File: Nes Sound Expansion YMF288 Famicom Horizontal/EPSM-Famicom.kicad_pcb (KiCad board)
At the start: 4 copper layers, 99 x 91.7 mm, 60 parts, among them J1 CARTRIDGE_F, J2 OUT_1, J3 EPSM_ADDRESSING, J4 CONSOLE_M, J5 AudioJack4_SwitchTR1, U1 74LS174, U10 74LS257, U2 74LS174, U3 74LS139, U4 74LS132, U5 YMF288, U6 BU9480F, U7 74LS257, U8 74LS257, U9 LM358, X1 SG-8002CA

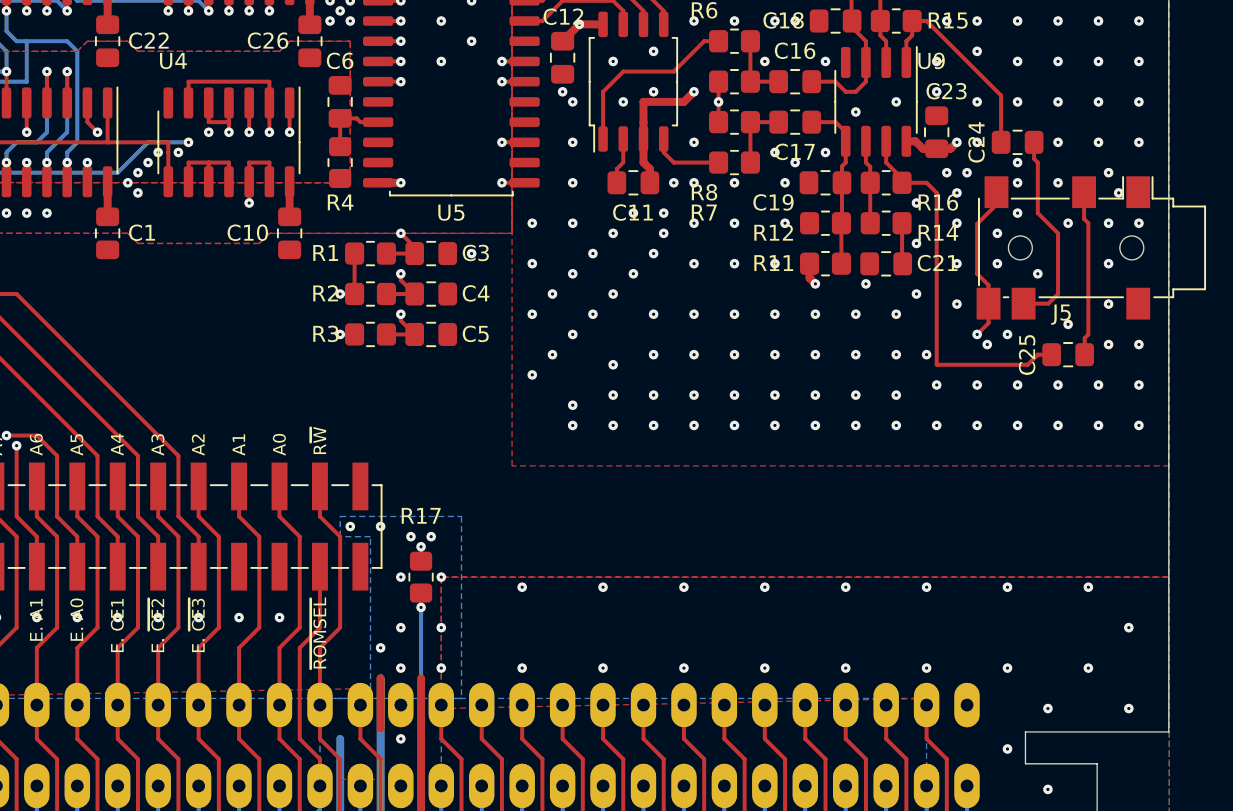
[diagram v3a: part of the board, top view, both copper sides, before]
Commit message: Clarify EPSM chip enable and address net names
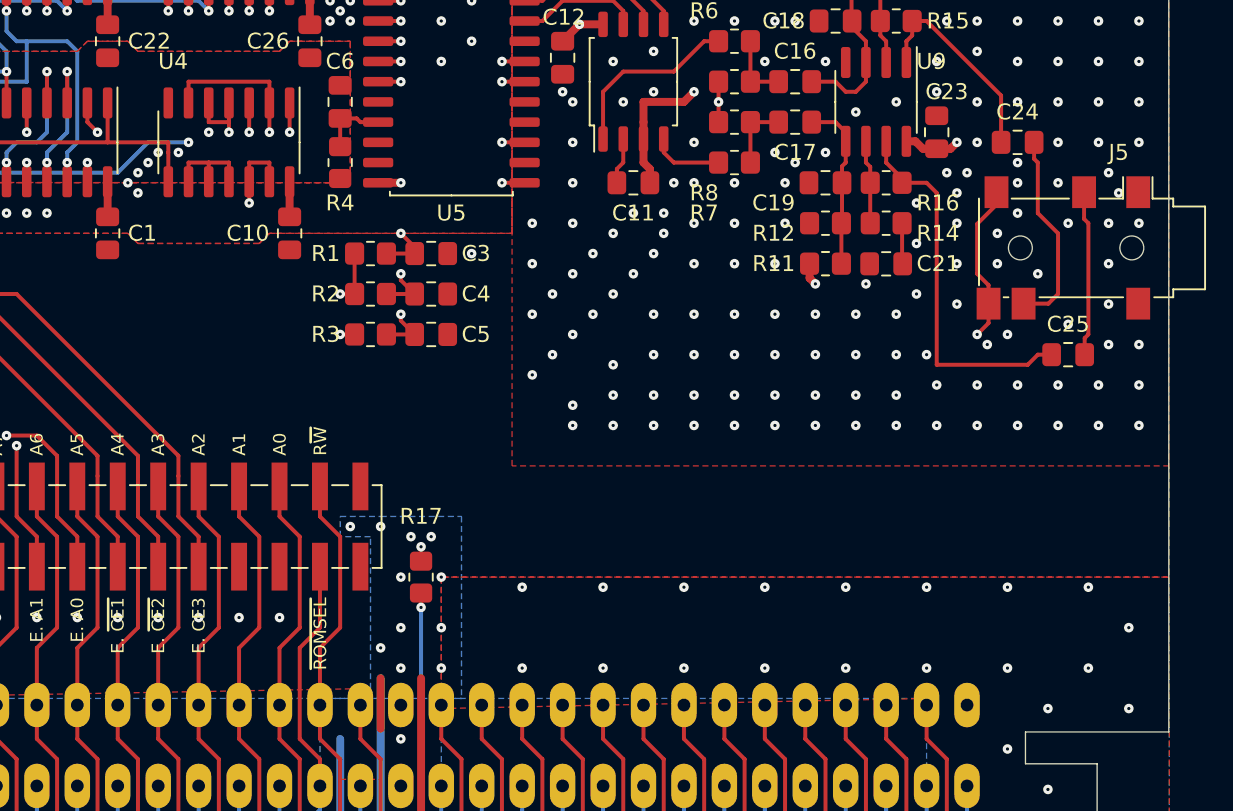
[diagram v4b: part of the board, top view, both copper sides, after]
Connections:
- net /EPSM_A0_A13 renamed /EPSM_A0
- net /EPSM_A1_A1 renamed /EPSM_A1
- net /EPSM_CE1_A14 renamed /EPSM_~{CE1}
- net /EPSM_CE2_~{ROMSEL} renamed /EPSM_~{CE2}
- net /EPSM_CE3_CPU_R~{W} renamed /EPSM_CE3
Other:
- board text added: "VCC M2 A12 A13 A14 E. A1 E. A0 E. ~{CE1} E. ~{CE2} E. CE3 ~{ROMSEL}"
- board text removed: "VCC M2 A12 A13 A14 E. A1 E. A0 E. CE1 E. ~{CE2} E. ~{CE3} ~{ROMSEL}"
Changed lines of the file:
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@@
   (net 62 "/OUT_1")
   (net 63 "unconnected-(J3-Pad24)")
-  (net 64 "/EPSM_A1_A1")
-  (net 65 "/EPSM_A0_A13")
-  (net 66 "/EPSM_CE1_A14")
-  (net 67 "/EPSM_CE2_~{ROMSEL}")
-  (net 68 "/EPSM_CE3_CPU_R~{W}")
+  (net 64 "/EPSM_A1")
+  (net 65 "/EPSM_A0")
+  (net 66 "/EPSM_~{CE1}")
+  (net 67 "/EPSM_~{CE2}")
+  (net 68 "/EPSM_CE3")
   (net 69 "unconnected-(J3-Pad26)")
   (net 70 "unconnected-(J3-Pad29)")
@@
     (fp_line (start -0.975 -4.95) (end 1.95 -4.95) (layer "F.Fab") (width 0.1))
     (pad "1" smd roundrect (at -2.475 -4.445 270) (size 1.95 0.6) (layers "F.Cu" "F.Paste" "F.Mask") (roundrect_rratio 0.25)
-      (net 67 "/EPSM_CE2_~{ROMSEL}") (pinfunction "E") (pintype "input"))
+      (net 67 "/EPSM_~{CE2}") (pinfunction "E") (pintype "input"))
     (pad "2" smd roundrect (at -2.475 -3.175 270) (size 1.95 0.6) (layers "F.Cu" "F.Paste" "F.Mask") (roundrect_rratio 0.25)
-      (net 66 "/EPSM_CE1_A14") (pinfunction "A0") (pintype "input"))
+      (net 66 "/EPSM_~{CE1}") (pinfunction "A0") (pintype "input"))
     (pad "3" smd roundrect (at -2.475 -1.905 270) (size 1.95 0.6) (layers "F.Cu" "F.Paste" "F.Mask") (roundrect_rratio 0.25)
-      (net 68 "/EPSM_CE3_CPU_R~{W}") (pinfunction "A1") (pintype "input"))
+      (net 68 "/EPSM_CE3") (pinfunction "A1") (pintype "input"))
     (pad "4" smd roundrect (at -2.475 -0.635 270) (size 1.95 0.6) (layers "F.Cu" "F.Paste" "F.Mask") (roundrect_rratio 0.25)
       (net 76 "unconnected-(U3-Pad4)") (pinfunction "O0") (pintype "output+no_connect"))
@@
       (net 7 "/CPU_A6") (pinfunction "Pin_13") (pintype "passive"))
     (pad "14" smd rect (at -2.52 -2.54 90) (size 3 1) (layers "F.Cu" "F.Paste" "F.Mask")
-      (net 64 "/EPSM_A1_A1") (pinfunction "Pin_14") (pintype "passive"))
+      (net 64 "/EPSM_A1") (pinfunction "Pin_14") (pintype "passive"))
     (pad "15" smd rect (at 2.52 0 90) (size 3 1) (layers "F.Cu" "F.Paste" "F.Mask")
       (net 8 "/CPU_A5") (pinfunction "Pin_15") (pintype "passive"))
     (pad "16" smd rect (at -2.52 0 90) (size 3 1) (layers "F.Cu" "F.Paste" "F.Mask")
-      (net 65 "/EPSM_A0_A13") (pinfunction "Pin_16") (pintype "passive"))
+      (net 65 "/EPSM_A0") (pinfunction "Pin_16") (pintype "passive"))
     (pad "17" smd rect (at 2.52 2.54 90) (size 3 1) (layers "F.Cu" "F.Paste" "F.Mask")
       (net 9 "/CPU_A4") (pinfunction "Pin_17") (pintype "passive"))
     (pad "18" smd rect (at -2.52 2.54 90) (size 3 1) (layers "F.Cu" "F.Paste" "F.Mask")
-      (net 66 "/EPSM_CE1_A14") (pinfunction "Pin_18") (pintype "passive"))
+      (net 66 "/EPSM_~{CE1}") (pinfunction "Pin_18") (pintype "passive"))
     (pad "19" smd rect (at 2.52 5.08 90) (size 3 1) (layers "F.Cu" "F.Paste" "F.Mask")
       (net 10 "/CPU_A3") (pinfunction "Pin_19") (pintype "passive"))
     (pad "20" smd rect (at -2.52 5.08 90) (size 3 1) (layers "F.Cu" "F.Paste" "F.Mask")
-      (net 67 "/EPSM_CE2_~{ROMSEL}") (pinfunction "Pin_20") (pintype "passive"))
+      (net 67 "/EPSM_~{CE2}") (pinfunction "Pin_20") (pintype "passive"))
     (pad "21" smd rect (at 2.52 7.62 90) (size 3 1) (layers "F.Cu" "F.Paste" "F.Mask")
       (net 11 "/CPU_A2") (pinfunction "Pin_21") (pintype "passive"))
     (pad "22" smd rect (at -2.52 7.62 90) (size 3 1) (layers "F.Cu" "F.Paste" "F.Mask")
-      (net 68 "/EPSM_CE3_CPU_R~{W}") (pinfunction "Pin_22") (pintype "passive"))
+      (net 68 "/EPSM_CE3") (pinfunction "Pin_22") (pintype "passive"))
     (pad "23" smd rect (at 2.52 10.16 90) (size 3 1) (layers "F.Cu" "F.Paste" "F.Mask")
       (net 12 "/CPU_A1") (pinfunction "Pin_23") (pintype "passive"))
@@
     (property "Sheetname" "")
     (attr smd)
-    (fp_text reference "C25" (at -2.54 0 90) (layer "F.SilkS")
+    (fp_text reference "C25" (at 0 -1.905 180) (layer "F.SilkS")
       (effects (font (size 1 1) (thickness 0.15)))
     )
@@
     (property "Sheetname" "")
     (attr smd)
-    (fp_text reference "J5" (at 4.09 6.955) (layer "F.SilkS")
+    (fp_text reference "J5" (at -5.995 3.425) (layer "F.SilkS")
       (effects (font (size 1 1) (thickness 0.15)))
     )
@@
       (net 73 "/$4016_EN") (pinfunction "S") (pintype "input"))
     (pad "2" smd roundrect (at -2.475 -3.175 270) (size 1.95 0.6) (layers "F.Cu" "F.Paste" "F.Mask") (roundrect_rratio 0.25)
-      (net 64 "/EPSM_A1_A1") (pinfunction "I0a") (pintype "input"))
+      (net 64 "/EPSM_A1") (pinfunction "I0a") (pintype "input"))
     (pad "3" smd roundrect (at -2.475 -1.905 270) (size 1.95 0.6) (layers "F.Cu" "F.Paste" "F.Mask") (roundrect_rratio 0.25)
       (net 107 "/BUF_A0") (pinfunction "I1a") (pintype "input"))
@@
       (net 108 "/YM_A1") (pinfunction "Za") (pintype "tri_state"))
     (pad "5" smd roundrect (at -2.475 0.635 270) (size 1.95 0.6) (layers "F.Cu" "F.Paste" "F.Mask") (roundrect_rratio 0.25)
-      (net 65 "/EPSM_A0_A13") (pinfunction "I0b") (pintype "input"))
+      (net 65 "/EPSM_A0") (pinfunction "I0b") (pintype "input"))
     (pad "6" smd roundrect (at -2.475 1.905 270) (size 1.95 0.6) (layers "F.Cu" "F.Paste" "F.Mask") (roundrect_rratio 0.25)
       (net 105 "/BUF_A1") (pinfunction "I1b") (pintype "input"))
@@
     (property "Sheetname" "")
     (attr smd)
-    (fp_text reference "C24" (at -2.54 0 90) (layer "F.SilkS")
+    (fp_text reference "C24" (at 0 -1.905 180) (layer "F.SilkS")
       (effects (font (size 1 1) (thickness 0.15)))
     )
@@
     (effects (font (size 1 1) (thickness 0.15)) (justify mirror))
   )
-  (gr_text "VCC\n\nM2\n\nA12\n\nA13\n\nA14\n\n \n\nE. A1\n\nE. A0\n\nE. CE1\n\nE. ~{CE2}\n\nE. ~{CE3}\n\n \n\n \n\n~{ROMSEL}\n\n " (at 107.95 93.345 90) (layer "F.SilkS")
+  (gr_text "VCC\n\nM2\n\nA12\n\nA13\n\nA14\n\n \n\nE. A1\n\nE. A0\n\nE. ~{CE1}\n\nE. ~{CE2}\n\nE. CE3\n\n \n\n \n\n~{ROMSEL}\n\n " (at 107.95 93.345 90) (layer "F.SilkS")
     (effects (font (size 0.79 0.8) (thickness 0.15875)) (justify right))
   )
@@
   (segment (start 110.49 89.535) (end 109.22 88.265) (width 0.25) (layer "F.Cu") (net 66))
   (segment (start 95.885 77.47) (end 95.25 76.835) (width 0.25) (layer "F.Cu") (net 66))
-  (segment (start 109.22 88.265) (end 109.22 84.455) (width 0.25) (layer "F.Cu") (net 66))
+  (segment (start 109.22 85.725) (end 109.22 84.455) (width 0.25) (layer "F.Cu") (net 66))
+  (segment (start 109.22 88.265) (end 109.22 85.725) (width 0.25) (layer "F.Cu") (net 66))
   (segment (start 96.52 75.63) (end 102.935 75.63) (width 0.25) (layer "F.Cu") (net 67))
-  (segment (start 111.76 84.455) (end 111.76 88.265) (width 0.25) (layer "F.Cu") (net 67))
   (segment (start 102.935 75.63) (end 111.76 84.455) (width 0.25) (layer "F.Cu") (net 67))
   (segment (start 111.76 88.265) (end 113.03 89.535) (width 0.25) (layer "F.Cu") (net 67))
   (segment (start 113.03 89.535) (end 113.03 91.42) (width 0.25) (layer "F.Cu") (net 67))
+  (segment (start 111.76 84.455) (end 111.76 85.725) (width 0.25) (layer "F.Cu") (net 67))
+  (segment (start 111.76 85.725) (end 111.76 88.265) (width 0.25) (layer "F.Cu") (net 67))
   (segment (start 96.52 74.295) (end 104.14 74.295) (width 0.25) (layer "F.Cu") (net 68))
-  (segment (start 114.3 84.455) (end 114.3 88.265) (width 0.25) (layer "F.Cu") (net 68))
+  (segment (start 114.3 84.455) (end 114.3 85.725) (width 0.25) (layer "F.Cu") (net 68))
+  (segment (start 114.3 85.725) (end 114.3 88.265) (width 0.25) (layer "F.Cu") (net 68))
   (segment (start 93.98 75.63) (end 93.98 74.295) (width 0.25) (layer "F.Cu") (net 68))
   (segment (start 114.3 88.265) (end 115.57 89.535) (width 0.25) (layer "F.Cu") (net 68))
